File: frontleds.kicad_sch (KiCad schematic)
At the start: 12 parts, among them IC1 STCS1APUR, IC2 STCS1APUR, J1 Conn_02x10_Odd_Even, J2 Conn_02x10_Odd_Even

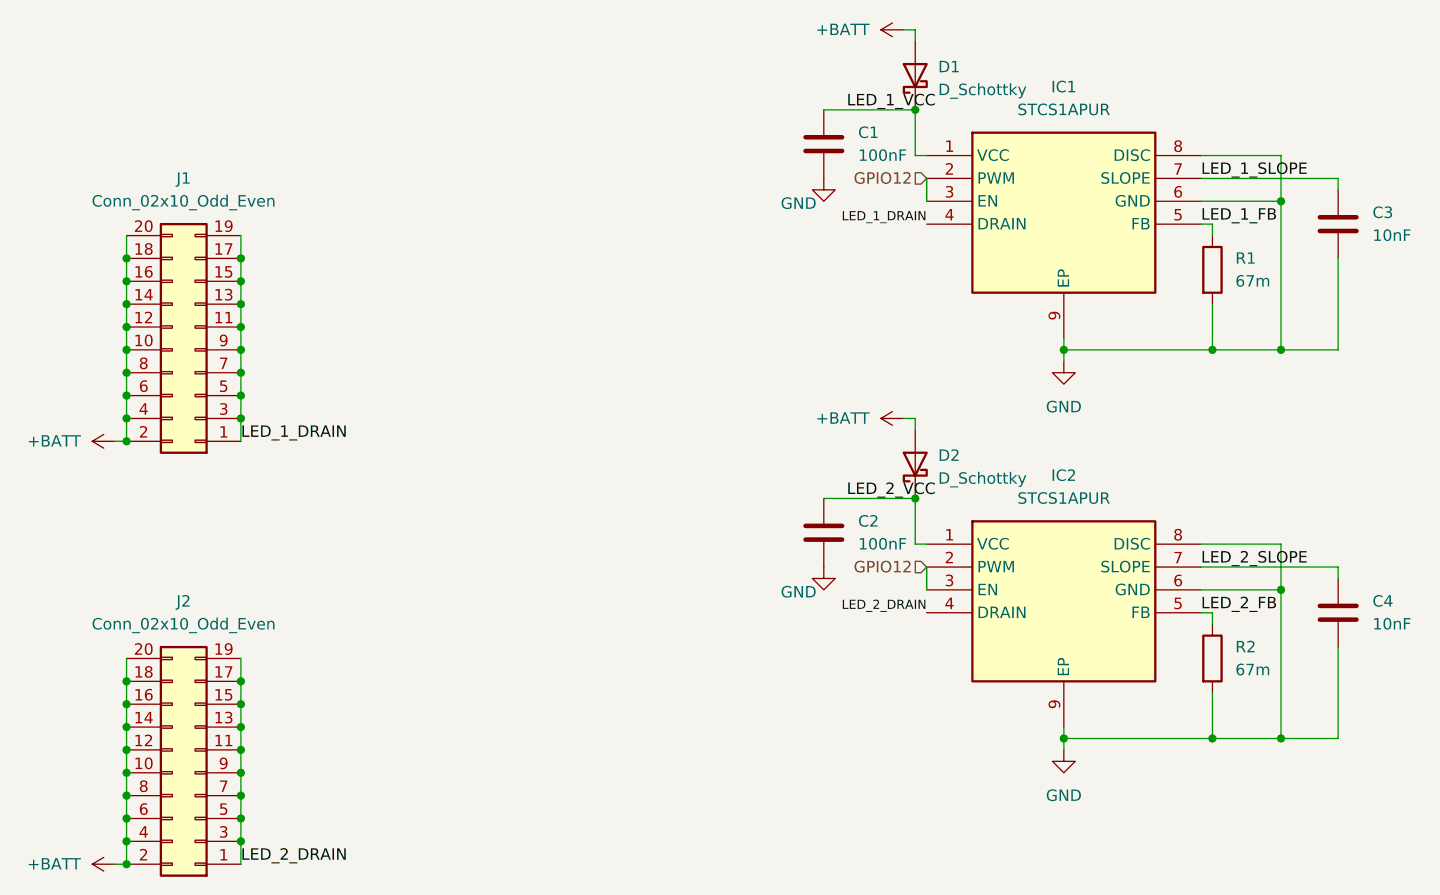
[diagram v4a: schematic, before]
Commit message: moved polyfuse to positive side of battery
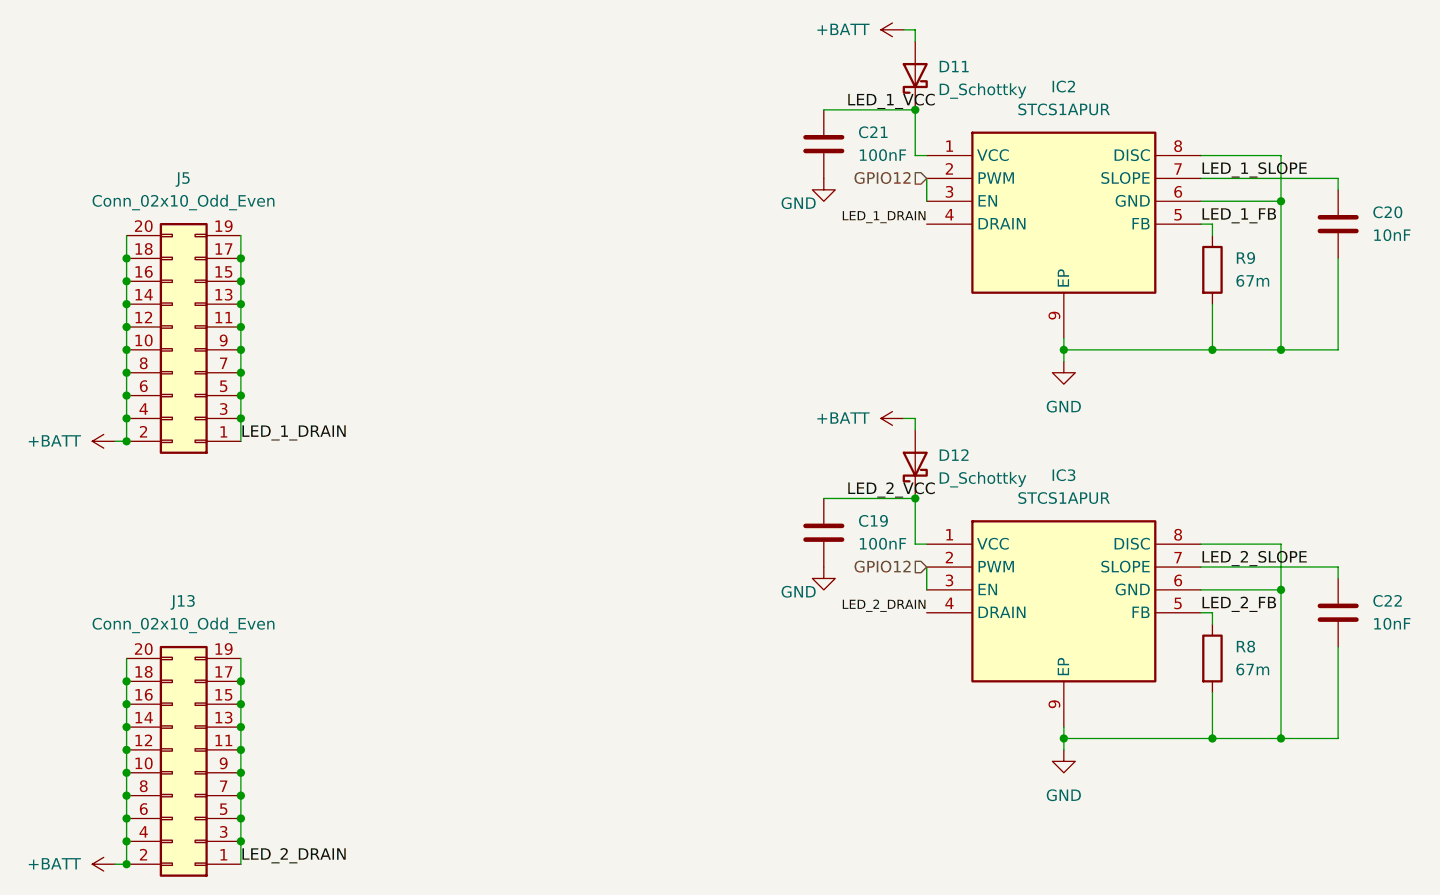
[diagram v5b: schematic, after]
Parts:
- renumbered C2 to C19, C3 to C20, C1 to C21, C4 to C22, D1 to D11, D2 to D12, IC1 to IC2, IC2 to IC3, J2 to J13, J1 to J5, R2 to R8, R1 to R9
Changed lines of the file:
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@@
 		(dnp no)
 		(fields_autoplaced yes)
-		(property "Reference" "#PWR05"
+		(property "Reference" "#PWR025"
 			(at 135.89 15.24 0)
 			(effects
@@
 		(dnp no)
 		(fields_autoplaced yes)
-		(property "Reference" "D2"
+		(property "Reference" "D12"
 			(at 135.89 62.5474 90)
 			(effects
@@
 		(dnp no)
 		(fields_autoplaced yes)
-		(property "Reference" "#PWR02"
+		(property "Reference" "#PWR027"
 			(at 48.26 107.95 0)
 			(effects
@@
 		(dnp no)
 		(fields_autoplaced yes)
-		(property "Reference" "#PWR07"
+		(property "Reference" "#PWR023"
 			(at 149.86 58.42 0)
 			(effects
@@
 		(dnp no)
 		(fields_autoplaced yes)
-		(property "Reference" "R1"
+		(property "Reference" "R9"
 			(at 168.91 40.6399 0)
 			(effects
@@
 		(on_board yes)
 		(dnp no)
-		(property "Reference" "#PWR03"
+		(property "Reference" "#PWR026"
 			(at 123.19 38.1 0)
 			(effects
@@
 		(dnp no)
 		(fields_autoplaced yes)
-		(property "Reference" "J2"
+		(property "Reference" "J13"
 			(at 52.07 78.74 0)
 			(effects
@@
 		(dnp no)
 		(fields_autoplaced yes)
-		(property "Reference" "IC2"
+		(property "Reference" "IC3"
 			(at 149.86 64.77 0)
 			(effects
@@
 		(dnp no)
 		(fields_autoplaced yes)
-		(property "Reference" "IC1"
+		(property "Reference" "IC2"
 			(at 149.86 21.59 0)
 			(effects
@@
 		(dnp no)
 		(fields_autoplaced yes)
-		(property "Reference" "C3"
+		(property "Reference" "C20"
 			(at 184.15 35.5599 0)
 			(effects
@@
 		(dnp no)
 		(fields_autoplaced yes)
-		(property "Reference" "C2"
+		(property "Reference" "C19"
 			(at 127 69.8499 0)
 			(effects
@@
 		(dnp no)
 		(fields_autoplaced yes)
-		(property "Reference" "C4"
+		(property "Reference" "C22"
 			(at 184.15 78.7399 0)
 			(effects
@@
 		(on_board yes)
 		(dnp no)
-		(property "Reference" "#PWR04"
+		(property "Reference" "#PWR021"
 			(at 123.19 81.28 0)
 			(effects
@@
 		(dnp no)
 		(fields_autoplaced yes)
-		(property "Reference" "#PWR08"
+		(property "Reference" "#PWR024"
 			(at 149.86 101.6 0)
 			(effects
@@
 		(dnp no)
 		(fields_autoplaced yes)
-		(property "Reference" "D1"
+		(property "Reference" "D11"
 			(at 135.89 19.3674 90)
 			(effects
@@
 		(dnp no)
 		(fields_autoplaced yes)
-		(property "Reference" "C1"
+		(property "Reference" "C21"
 			(at 127 26.6699 0)
 			(effects
@@
 		(dnp no)
 		(fields_autoplaced yes)
-		(property "Reference" "#PWR06"
+		(property "Reference" "#PWR022"
 			(at 135.89 58.42 0)
 			(effects
@@
 		(dnp no)
 		(fields_autoplaced yes)
-		(property "Reference" "#PWR01"
+		(property "Reference" "#PWR020"
 			(at 48.26 60.96 0)
 			(effects
@@
 		(dnp no)
 		(fields_autoplaced yes)
-		(property "Reference" "R2"
+		(property "Reference" "R8"
 			(at 168.91 83.8199 0)
 			(effects
@@
 		(dnp no)
 		(fields_autoplaced yes)
-		(property "Reference" "J1"
+		(property "Reference" "J5"
 			(at 52.07 31.75 0)
 			(effects

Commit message: lcsc part numbers
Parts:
- IC2, IC3: LCSC (none) -> C2971041
- J13, J5: LCSC (none) -> C4572809
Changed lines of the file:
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@@
+			)
+		)
+		(property "LCSC" "C4572809"
+			(at 53.34 97.79 0)
+			(effects
+				(font
+					(size 1.27 1.27)
+				)
+				(hide yes)
 			)
 		)
@@
 			)
 		)
+		(property "LCSC" "C2971041"
+			(at 134.62 72.39 0)
+			(effects
+				(font
+					(size 1.27 1.27)
+				)
+				(hide yes)
+			)
+		)
 		(pin "3"
 		)
@@
 			)
 		)
+		(property "LCSC" "C2971041"
+			(at 134.62 29.21 0)
+			(effects
+				(font
+					(size 1.27 1.27)
+				)
+				(hide yes)
+			)
+		)
 		(pin "3"
 		)
@@
 			(at 53.34 50.8 0)
 			(effects
+				(font
+					(size 1.27 1.27)
+				)
+				(hide yes)
+			)
+		)
+		(property "LCSC" "C4572809"
+			(at 53.34 50.8 0)
+			(effects

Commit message: more lcsc
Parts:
- C19, C21: LCSC (none) -> C1525
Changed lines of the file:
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@@
+			)
+		)
+		(property "LCSC" "C1525"
+			(at 123.19 71.12 0)
+			(effects
+				(font
+					(size 1.27 1.27)
+				)
+				(hide yes)
 			)
 		)
@@
 			(at 123.19 27.94 0)
 			(effects
+				(font
+					(size 1.27 1.27)
+				)
+				(hide yes)
+			)
+		)
+		(property "LCSC" "C1525"
+			(at 123.19 27.94 0)
+			(effects

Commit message: lcsc resistors and capacitors done probably except the 67m one
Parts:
- C20, C22: LCSC (none) -> C15195
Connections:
- net GND: now also C20.1; no longer C20.2
- net LED_1_SLOPE: now also C20.2; no longer C20.1
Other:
- moved on the sheet: C20
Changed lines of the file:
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@@
 	(symbol
 		(lib_id "Device:C")
-		(at 180.34 36.83 0)
+		(at 180.34 36.83 180)
 		(unit 1)
 		(exclude_from_sim no)
@@
 					(size 1.27 1.27)
 				)
-				(justify left)
+				(justify right)
 			)
 		)
@@
 					(size 1.27 1.27)
 				)
-				(justify left)
+				(justify right)
 			)
 		)
 		(property "Footprint" "Capacitor_SMD:C_0402_1005Metric"
-			(at 181.3052 40.64 0)
+			(at 179.3748 33.02 0)
 			(effects
 				(font
@@
 		)
 		(property "Description" "Unpolarized capacitor"
+			(at 180.34 36.83 0)
+			(effects
+				(font
+					(size 1.27 1.27)
+				)
+				(hide yes)
+			)
+		)
+		(property "LCSC" "C15195"
 			(at 180.34 36.83 0)
 			(effects
@@
 			(at 180.34 80.01 0)
 			(effects
+				(font
+					(size 1.27 1.27)
+				)
+				(hide yes)
+			)
+		)
+		(property "LCSC" "C15195"
+			(at 180.34 80.01 0)
+			(effects
